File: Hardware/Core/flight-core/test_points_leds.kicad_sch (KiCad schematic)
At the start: 0 parts

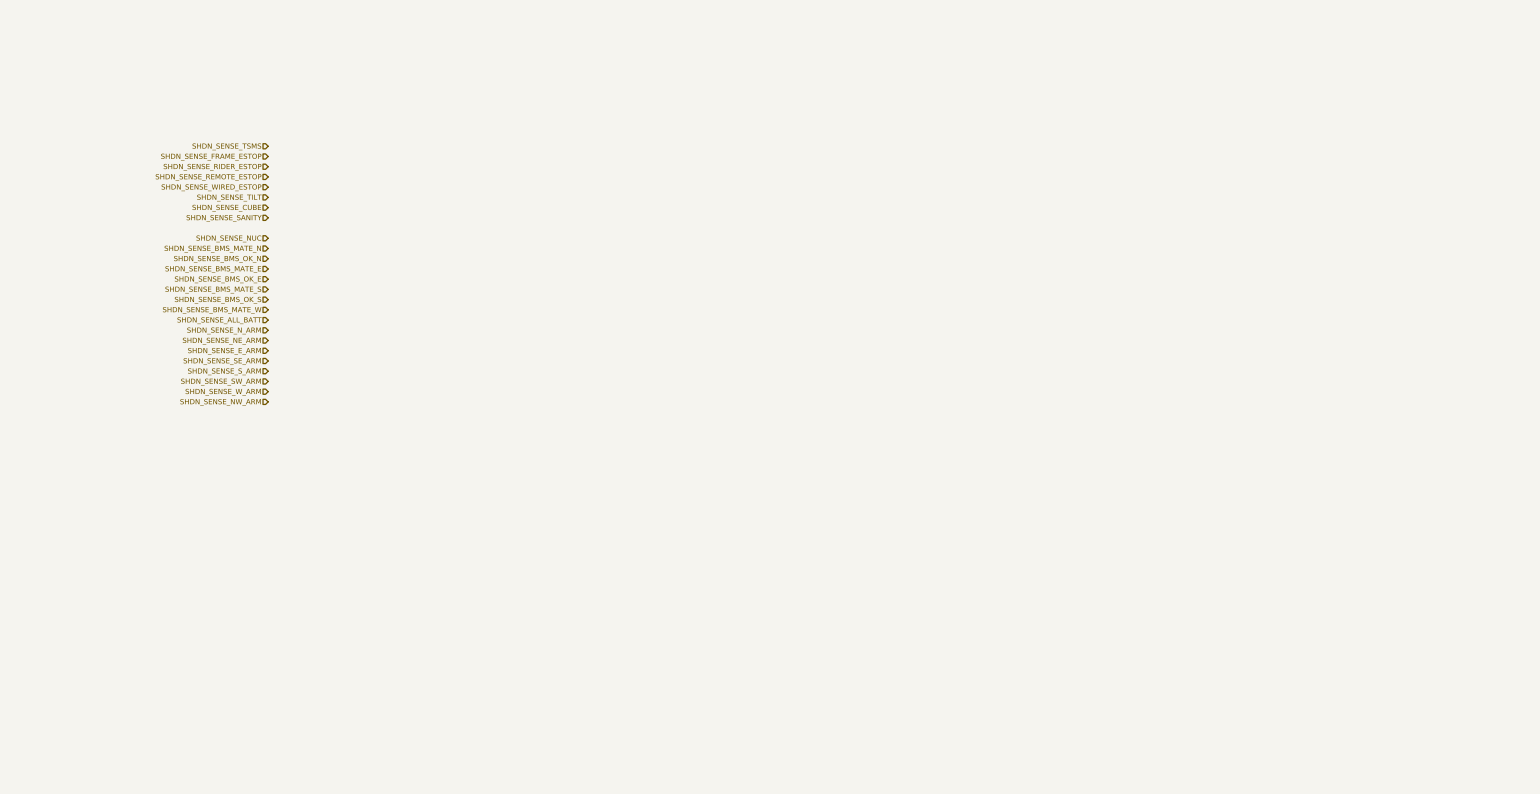
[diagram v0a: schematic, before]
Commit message: added test points and LEDs; color inaccurate
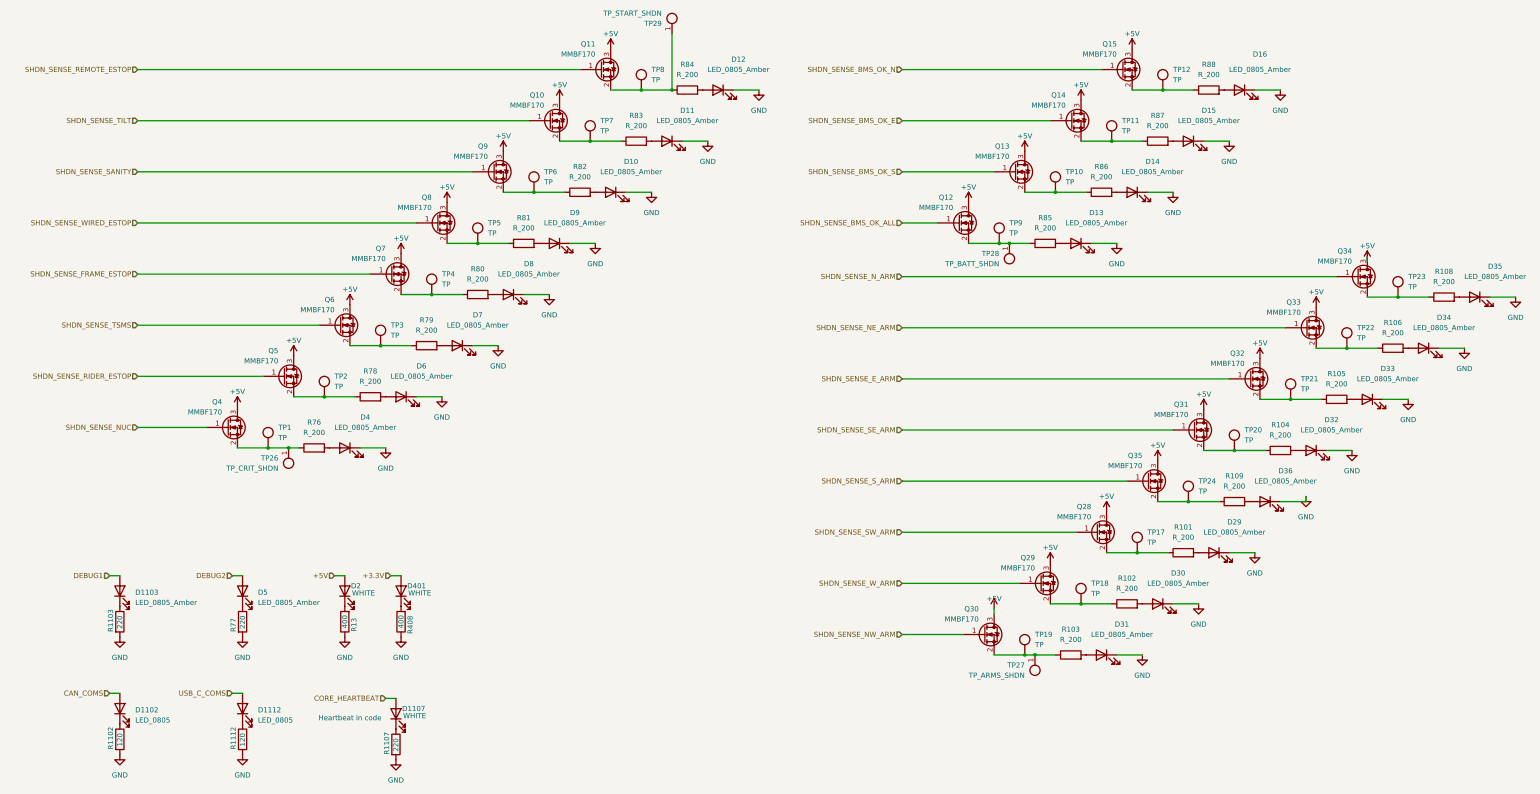
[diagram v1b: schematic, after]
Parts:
- added D10, D11, D1103, D12, D13, D14, D15, D16, D29, D30, D31, D32, D33, D34, D35, D36, D4, D5, D6, D7, D8, D9: LED_0805_Amber, footprints:LED_0805_OEM, symbol formula:LED_0805_Amber
- added D1102, D1112: LED_0805, footprints:LED_0805_OEM, symbol formula:LED_0805
- added D1107, D2, D401: WHITE, LED_SMD:LED_0805_2012Metric, symbol Device:LED
- added Q10, Q11, Q12, Q13, Q14, Q15, Q28, Q29, Q30, Q31, Q32, Q33, Q34, Q35, Q4, Q5, Q6, Q7, Q8, Q9: MMBF170, TO_SOT_Packages_SMD:SOT-23, symbol formula:MMBF170
- added R101, R102, R103, R104, R105, R106, R108, R109, R76, R78, R79, R80, R81, R82, R83, R84, R85, R86, R87, R88: R_200, footprints:R_0603_1608Metric, symbol formula:R_200
- added R1102, R1112: 120, OEM:R_0603_1608Metric, symbol OEM:120R_DNP
- added R1103, R1107, R77: 220, OEM:R_0603_1608Metric, symbol OEM:120R_DNP
- added R13, R408: 400, Resistor_SMD:R_0603_1608Metric, symbol Device:R
- added TP1, TP10, TP11, TP12, TP17, TP18, TP19, TP2, TP20, TP21, TP22, TP23, TP24, TP3, TP4, TP5, TP6, TP7, TP8, TP9: TP, footprints:tp_1.6mm, symbol formula:TP
- added TP26: TP_CRIT_SHDN, footprints:Test_Point_SMD, symbol formula:TP_SMD
- added TP27: TP_ARMS_SHDN, footprints:Test_Point_SMD, symbol formula:TP_SMD
- added TP28: TP_BATT_SHDN, footprints:Test_Point_SMD, symbol formula:TP_SMD
- added TP29: TP_START_SHDN, footprints:Test_Point_SMD, symbol formula:TP_SMD
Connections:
- net SHDN_SENSE_BMS_OK_E: now also Q14.1 (G)
- net SHDN_SENSE_BMS_OK_N: now also Q15.1 (G)
- net SHDN_SENSE_BMS_OK_S: now also Q13.1 (G)
- net SHDN_SENSE_E_ARM: now also Q32.1 (G)
- net SHDN_SENSE_FRAME_ESTOP: now also Q7.1 (G)
- net SHDN_SENSE_NE_ARM: now also Q33.1 (G)
- net SHDN_SENSE_NUC: now also Q4.1 (G)
- net SHDN_SENSE_NW_ARM: now also Q30.1 (G)
- net SHDN_SENSE_N_ARM: now also Q34.1 (G)
- net SHDN_SENSE_REMOTE_ESTOP: now also Q11.1 (G)
- net SHDN_SENSE_RIDER_ESTOP: now also Q5.1 (G)
- net SHDN_SENSE_SANITY: now also Q9.1 (G)
- net SHDN_SENSE_SE_ARM: now also Q31.1 (G)
- net SHDN_SENSE_SW_ARM: now also Q28.1 (G)
- net SHDN_SENSE_S_ARM: now also Q35.1 (G)
- net SHDN_SENSE_TILT: now also Q10.1 (G)
- net SHDN_SENSE_TSMS: now also Q6.1 (G)
- net SHDN_SENSE_WIRED_ESTOP: now also Q8.1 (G)
- net SHDN_SENSE_W_ARM: now also Q29.1 (G)
- new net: Q28.2 (S), R101.1, TP17.1 (TP)
- new net: Q5.2 (S), R78.1, TP2.1 (TP)
- new net: D9.2 (A), R81.2
- new net: D401.1 (K), R408.2
- new net: D1103.1 (K), R1103.1
- new net: D2.1 (K), R13.2
- new net: Q6.2 (S), R79.1, TP3.1 (TP)
- new net: Q4.2 (S), R76.1, TP1.1 (TP), TP26.1
- new net: Q11.2 (S), R84.1, TP29.1, TP8.1 (TP)
- new net: Q13.2 (S), R86.1, TP10.1 (TP)
- new net: D14.2 (A), R86.2
- new net: Q33.2 (S), R106.1, TP22.1 (TP)
- new net: D29.2 (A), R101.2
- new net: D30.2 (A), R102.2
- new net: Q12.2 (S), R85.1, TP28.1, TP9.1 (TP)
- new net: D35.2 (A), R108.2
- new net: Q30.2 (S), R103.1, TP19.1 (TP), TP27.1
- new net: D31.2 (A), R103.2
- new net: Q8.2 (S), R81.1, TP5.1 (TP)
- new net: D1112.1 (K), R1112.1
- new net: Q15.2 (S), R88.1, TP12.1 (TP)
- new net: Q31.2 (S), R104.1, TP20.1 (TP)
- new net: D32.2 (A), R104.2
- new net: Q29.2 (S), R102.1, TP18.1 (TP)
- new net: Q14.2 (S), R87.1, TP11.1 (TP)
- new net: D15.2 (A), R87.2
- new net: Q10.2 (S), R83.1, TP7.1 (TP)
- new net: D11.2 (A), R83.2
- new net: D13.2 (A), R85.2
- new net: Q35.2 (S), R109.1, TP24.1 (TP)
- new net: D4.2 (A), R76.2
- new net: D33.2 (A), R105.2
- new net: D36.2 (A), R109.2
- new net: D1107.1 (K), R1107.1
- new net: D34.2 (A), R106.2
- new net: D6.2 (A), R78.2
- new net: Q9.2 (S), R82.1, TP6.1 (TP)
- new net: D10.2 (A), R82.2
- new net: D12.2 (A), R84.2
- new net: Q34.2 (S), R108.1, TP23.1 (TP)
- new net: D1102.1 (K), R1102.1
- new net: Q7.2 (S), R80.1, TP4.1 (TP)
- new net: D5.1 (K), R77.1
- new net: Q32.2 (S), R105.1, TP21.1 (TP)
- new net: D16.2 (A), R88.2
- new net: D7.2 (A), R79.2
- new net: D8.2 (A), R80.2
- new net +3.3V: D401.2 (A)
- new net +5V: D2.2 (A), Q10.3 (D), Q11.3 (D), Q12.3 (D), Q13.3 (D), Q14.3 (D), Q15.3 (D), Q28.3 (D), Q29.3 (D), Q30.3 (D), Q31.3 (D), Q32.3 (D), Q33.3 (D), Q34.3 (D), Q35.3 (D), Q4.3 (D), Q5.3 (D), Q6.3 (D), Q7.3 (D), Q8.3 (D), Q9.3 (D)
- new net CAN_COMS: D1102.2 (A)
- new net CORE_HEARTBEAT: D1107.2 (A)
- new net DEBUG1: D1103.2 (A)
- new net DEBUG2: D5.2 (A)
- new net GND: D10.1 (K), D11.1 (K), D12.1 (K), D13.1 (K), D14.1 (K), D15.1 (K), D16.1 (K), D29.1 (K), D30.1 (K), D31.1 (K), D32.1 (K), D33.1 (K), D34.1 (K), D35.1 (K), D36.1 (K), D4.1 (K), D6.1 (K), D7.1 (K), D8.1 (K), D9.1 (K), R1102.2, R1103.2, R1107.2, R1112.2, R13.1, R408.1, R77.2
- new net SHDN_SENSE_BMS_OK_ALL: Q12.1 (G)
- new net USB_C_COMS: D1112.2 (A)
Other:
- note added: "Heartbeat in code"

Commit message: top sheet reorg
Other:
- moved on the sheet: D1102, D1103, D1107, D1112, D13, D14, D15, D16, D2, D29, D30, D31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

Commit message: updated all top sheets
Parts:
- added D23: WHITE, LED_SMD:LED_0805_2012Metric, symbol Device:LED
- added D24: LED_0805_Amber, footprints:LED_0805_OEM, symbol formula:LED_0805_Amber
- added Q20: MMBF170, TO_SOT_Packages_SMD:SOT-23, symbol formula:MMBF170
- added R11: 400, Resistor_SMD:R_0603_1608Metric, symbol Device:R
- added R12: R_200, footprints:R_0603_1608Metric, symbol formula:R_200
- added TP15: TP, footprints:tp_1.6mm, symbol formula:TP
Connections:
- net +5V: now also Q20.3 (D)
- net GND: now also D24.1 (K), R11.1
- net SHDN_SENSE_BMS_OK_ALL: now also TP28.1, TP9.1 (TP)
- net SHDN_SENSE_BMS_OK_E: now also TP11.1 (TP)
- net SHDN_SENSE_BMS_OK_N: now also TP12.1 (TP)
- net SHDN_SENSE_BMS_OK_S: now also TP10.1 (TP)
- net SHDN_SENSE_E_ARM: now also TP21.1 (TP)
- net SHDN_SENSE_FRAME_ESTOP: now also TP4.1 (TP)
- net SHDN_SENSE_NE_ARM: now also TP22.1 (TP)
- net SHDN_SENSE_NUC: now also TP1.1 (TP)
- net SHDN_SENSE_NW_ARM: now also TP19.1 (TP), TP27.1
- net SHDN_SENSE_N_ARM: now also TP23.1 (TP)
- net SHDN_SENSE_REMOTE_ESTOP: now also TP29.1, TP8.1 (TP)
- net SHDN_SENSE_RIDER_ESTOP: now also TP2.1 (TP), TP26.1
- net SHDN_SENSE_SE_ARM: now also TP20.1 (TP)
- net SHDN_SENSE_SW_ARM: now also TP17.1 (TP)
- net SHDN_SENSE_S_ARM: now also TP24.1 (TP)
- net SHDN_SENSE_TILT: now also TP7.1 (TP)
- net SHDN_SENSE_TSMS: now also TP3.1 (TP)
- net SHDN_SENSE_WIRED_ESTOP: now also TP5.1 (TP)
- net SHDN_SENSE_W_ARM: now also TP18.1 (TP)
- net at Q28.2 (S), R101.1: no longer TP17.1 (TP)
- net at Q5.2 (S), R78.1: no longer TP2.1 (TP)
- net at Q6.2 (S), R79.1: no longer TP3.1 (TP)
- net at Q4.2 (S), R76.1: no longer TP1.1 (TP), TP26.1
- net at Q11.2 (S), R84.1: no longer TP29.1, TP8.1 (TP)
- net at Q13.2 (S), R86.1: no longer TP10.1 (TP)
- net at Q33.2 (S), R106.1: no longer TP22.1 (TP)
- net at Q12.2 (S), R85.1: no longer TP28.1, TP9.1 (TP)
- net at Q30.2 (S), R103.1: no longer TP19.1 (TP), TP27.1
- net at Q8.2 (S), R81.1: no longer TP5.1 (TP)
- net at Q15.2 (S), R88.1: no longer TP12.1 (TP)
- net at Q31.2 (S), R104.1: no longer TP20.1 (TP)
- net at Q29.2 (S), R102.1: no longer TP18.1 (TP)
- net at Q14.2 (S), R87.1: no longer TP11.1 (TP)
- net at Q10.2 (S), R83.1: no longer TP7.1 (TP)
- net at Q35.2 (S), R109.1: no longer TP24.1 (TP)
- net at Q9.2 (S), R82.1: no longer TP6.1 (TP)
- net at Q34.2 (S), R108.1: no longer TP23.1 (TP)
- net at Q7.2 (S), R80.1: no longer TP4.1 (TP)
- net at Q32.2 (S), R105.1: no longer TP21.1 (TP)
- net SHDN_SENSE_SANITY renamed SHDN_SENSE_CTRL_CRIT
- net SHDN_SENSE_CTRL_CRIT: now also TP6.1 (TP)
- new net: Q20.2 (S), R12.1
- new net: D24.2 (A), R12.2
- new net: D23.1 (K), R11.2
- new net +60V: D23.2 (A)
- new net SHDN_SENSE_CTRL_LOBATT: Q20.1 (G), TP15.1 (TP)
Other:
- note added: "TPS ON SIGNAL LINE, CAN+/- GND +5V +3.3V +60V 5019S"
- moved on the sheet: D10, D11, D1102, D1103, D1107, D1112, D12, D13, D14, D15, D16, D2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

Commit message: minor erc fixes (grid, reannotation, updated footprint associations)
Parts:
- removed D1107, D2, D23, D401: WHITE, LED_SMD:LED_0805_2012Metric, symbol Device:LED
- removed R11, R13, R408: 400, Resistor_SMD:R_0603_1608Metric, symbol Device:R
- removed R1102, R1112: 120, OEM:R_0603_1608Metric, symbol OEM:120R_DNP
- removed R1103, R1107, R77: 220, OEM:R_0603_1608Metric, symbol OEM:120R_DNP
- added D14, D15, D18, D21: LED_0805_WHITE, footprints:LED_0805_OEM, symbol OlinBAD:LED_0805_WHITE
- added R59, R60, R61, R62, R63, R65, R67: 220, footprints:R_0603_1608Metric, symbol Device:R
- added R70: 3300, footprints:R_0603_1608Metric, symbol Device:R
- added TP_STM_IO1, TP_STM_IO2: TP, footprints:tp_1.6mm, symbol formula:TP
- Q10: renamed from Q6; footprint TO_SOT_Packages_SMD:SOT-23 -> Package_TO_SOT_SMD:SOT-23
- Q11: renamed from Q7; footprint TO_SOT_Packages_SMD:SOT-23 -> Package_TO_SOT_SMD:SOT-23
- Q12: renamed from Q8; footprint TO_SOT_Packages_SMD:SOT-23 -> Package_TO_SOT_SMD:SOT-23
- Q13: renamed from Q9; footprint TO_SOT_Packages_SMD:SOT-23 -> Package_TO_SOT_SMD:SOT-23
- Q14: renamed from Q10; footprint TO_SOT_Packages_SMD:SOT-23 -> Package_TO_SOT_SMD:SOT-23
- Q15: renamed from Q11; footprint TO_SOT_Packages_SMD:SOT-23 -> Package_TO_SOT_SMD:SOT-23
- Q16: renamed from Q30; footprint TO_SOT_Packages_SMD:SOT-23 -> Package_TO_SOT_SMD:SOT-23
- Q17: renamed from Q12; footprint TO_SOT_Packages_SMD:SOT-23 -> Package_TO_SOT_SMD:SOT-23
- Q18: renamed from Q29; footprint TO_SOT_Packages_SMD:SOT-23 -> Package_TO_SOT_SMD:SOT-23
- Q19: renamed from Q13; footprint TO_SOT_Packages_SMD:SOT-23 -> Package_TO_SOT_SMD:SOT-23
- Q20: renamed from Q28; footprint TO_SOT_Packages_SMD:SOT-23 -> Package_TO_SOT_SMD:SOT-23
- Q21: renamed from Q14; footprint TO_SOT_Packages_SMD:SOT-23 -> Package_TO_SOT_SMD:SOT-23
- Q22: renamed from Q35; footprint TO_SOT_Packages_SMD:SOT-23 -> Package_TO_SOT_SMD:SOT-23
- Q23: renamed from Q20; footprint TO_SOT_Packages_SMD:SOT-23 -> Package_TO_SOT_SMD:SOT-23
- Q24: renamed from Q4; footprint TO_SOT_Packages_SMD:SOT-23 -> Package_TO_SOT_SMD:SOT-23
- Q25: renamed from Q15; footprint TO_SOT_Packages_SMD:SOT-23 -> Package_TO_SOT_SMD:SOT-23
- Q26: renamed from Q31; footprint TO_SOT_Packages_SMD:SOT-23 -> Package_TO_SOT_SMD:SOT-23
- Q27: renamed from Q32; footprint TO_SOT_Packages_SMD:SOT-23 -> Package_TO_SOT_SMD:SOT-23
- Q28: renamed from Q33; footprint TO_SOT_Packages_SMD:SOT-23 -> Package_TO_SOT_SMD:SOT-23
- Q29: renamed from Q34; footprint TO_SOT_Packages_SMD:SOT-23 -> Package_TO_SOT_SMD:SOT-23
- Q9: renamed from Q5; footprint TO_SOT_Packages_SMD:SOT-23 -> Package_TO_SOT_SMD:SOT-23
- renumbered D1103 to D10, D1102 to D11, D5 to D12, D1112 to D13, D6 to D16, D7 to D17, D8 to D19, D9 to D20, D10 to D22, D11 to D23, D12 to D24, D31 to D25, D13 to D26, D30 to D27, D14 to D28, D15 to D30, D36 to D31, D24 to D32, D4 to D33, D16 to D34, D32 to D35, D33 to D36, D34 to D37, D35 to D38, R78 to R64, R79 to R66, R80 to R68, R81 to R69, R82 to R71, R83 to R72, R84 to R73, R103 to R74, R85 to R75, R102 to R76, R86 to R77, R101 to R78, R87 to R79, R109 to R80, R12 to R81, R76 to R82, R88 to R83, R104 to R84, R105 to R85, R106 to R86, R108 to R87, TP26 to TP10, TP3 to TP11, TP4 to TP12, TP5 to TP13, TP6 to TP14, TP7 to TP15, TP8 to TP16, TP29 to TP17, TP19 to TP18, TP9 to TP19, TP27 to TP20, TP28 to TP21, TP10 to TP22, TP18 to TP23, TP15 to TP24, TP1 to TP25, TP11 to TP26, TP17 to TP27, TP12 to TP28, TP24 to TP29, TP20 to TP30, TP21 to TP31, TP22 to TP32, TP23 to TP33, TP2 to TP9
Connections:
- net +3.3V: now also D18.2 (A)
- net +5V: now also D14.2 (A)
- net +60V: now also D21.2 (A)
- net CORE_HEARTBEAT: now also D15.2 (A)
- net DEBUG1: now also TP_STM_IO1.1 (TP)
- net DEBUG2: now also TP_STM_IO2.1 (TP)
- net GND: now also R59.1, R60.1, R61.1, R62.1, R63.1, R65.1, R67.1, R70.2
- net at D10.1 (K): now also R59.2
- net at D13.1 (K): now also R62.2
- net at D11.1 (K): now also R60.2
- net at D12.1 (K): now also R61.2
- new net: D21.1 (K), R70.1
- new net: D18.1 (K), R67.2
- new net: D15.1 (K), R65.2
- new net: D14.1 (K), R63.2
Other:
- note removed: "TPS ON SIGNAL LINE, CAN+/- GND +5V +3.3V +60V 5019S"
- moved on the sheet: D10, D11, D12, D13, D25, D26, D27, D28, D29, D30, D31, D34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

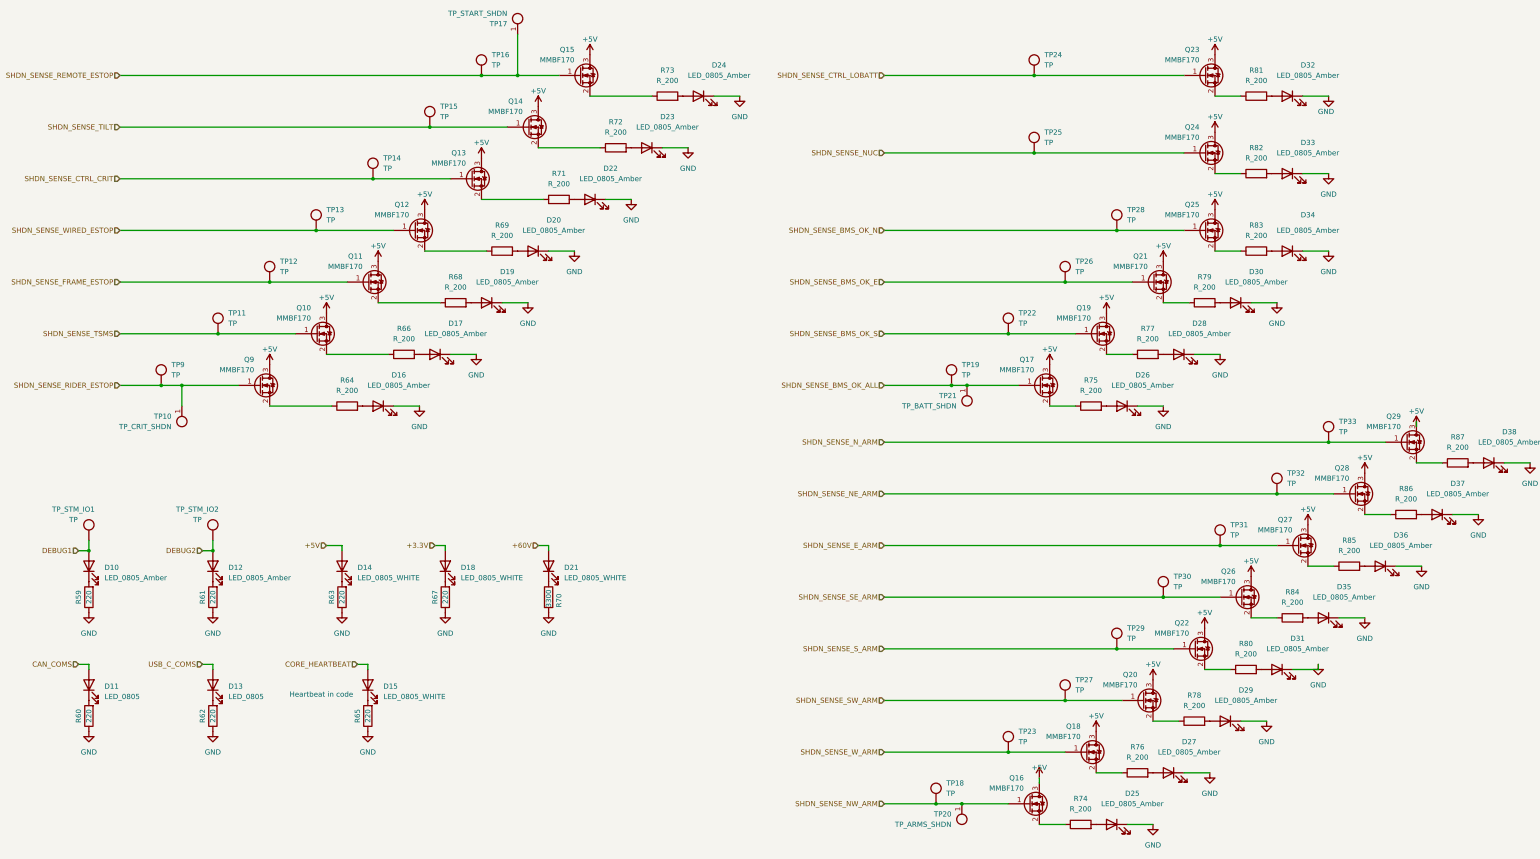
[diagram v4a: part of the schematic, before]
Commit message: added sense pwr cycle pull down, low side cube mosfets, fixed mosi/miso swap on i/o expander, Rs -> generic, reannotated
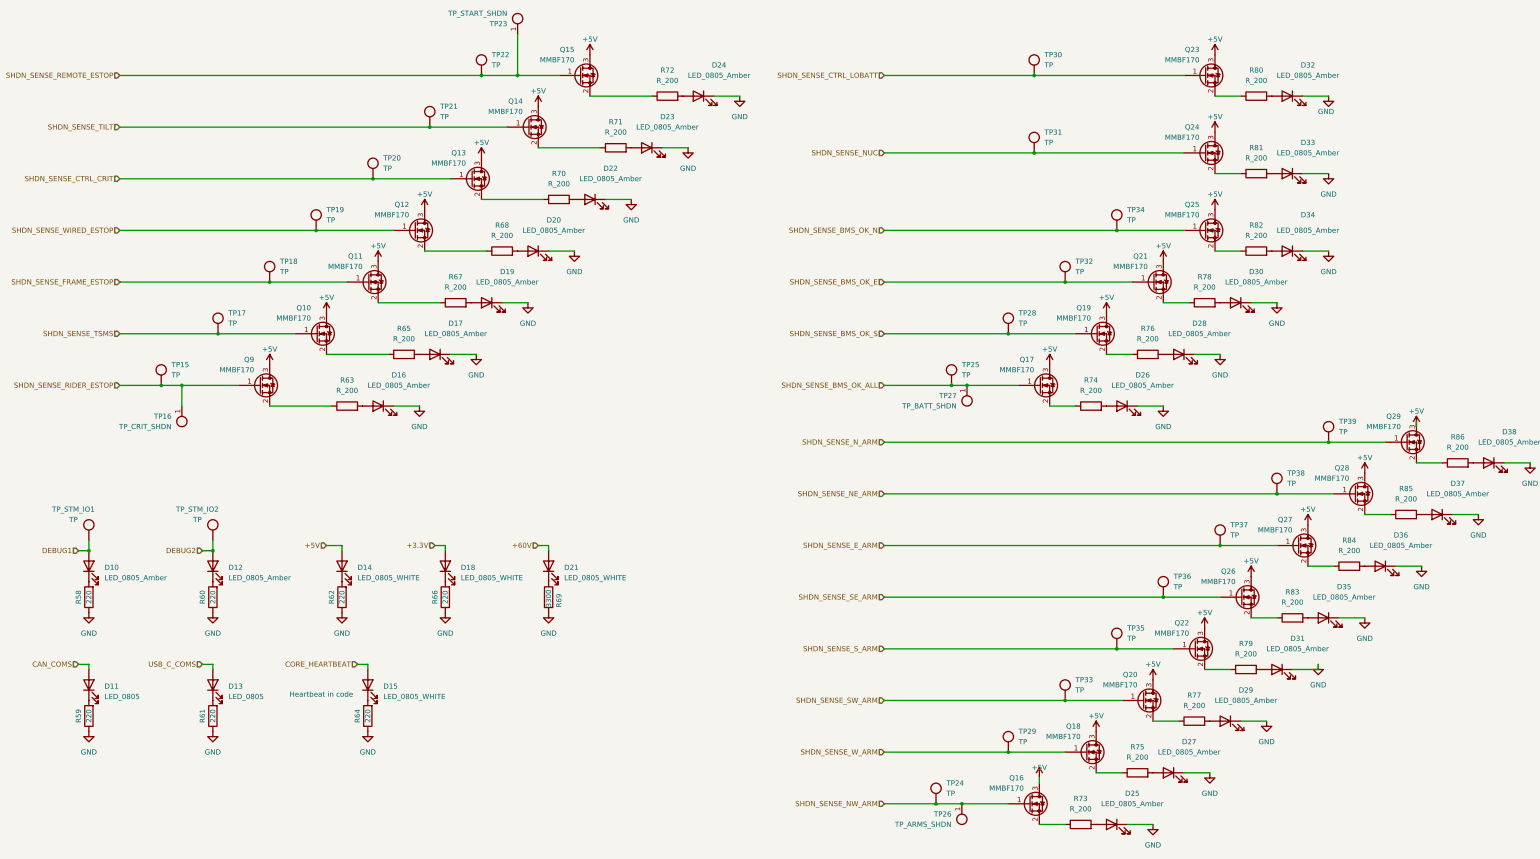
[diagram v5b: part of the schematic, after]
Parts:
- renumbered R59 to R58, R60 to R59, R61 to R60, R62 to R61, R63 to R62, R64 to R63, R65 to R64, R66 to R65, R67 to R66, R68 to R67, R69 to R68, R70 to R69, R71 to R70, R72 to R71, R73 to R72, R74 to R73, R75 to R74, R76 to R75, R77 to R76, R78 to R77, R79 to R78, R80 to R79, R81 to R80, R82 to R81, R83 to R82, R84 to R83, R85 to R84, R86 to R85, R87 to R86, TP9 to TP15, TP10 to TP16, TP11 to TP17, TP12 to TP18, TP13 to TP19, TP14 to TP20, TP15 to TP21, TP16 to TP22, TP17 to TP23, TP18 to TP24, TP19 to TP25, TP20 to TP26, TP21 to TP27, TP22 to TP28, TP23 to TP29, TP24 to TP30, TP25 to TP31, TP26 to TP32, TP27 to TP33, TP28 to TP34, TP29 to TP35, TP30 to TP36, TP31 to TP37, TP32 to TP38, TP33 to TP39
